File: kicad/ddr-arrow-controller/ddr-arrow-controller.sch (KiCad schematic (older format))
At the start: 50 parts

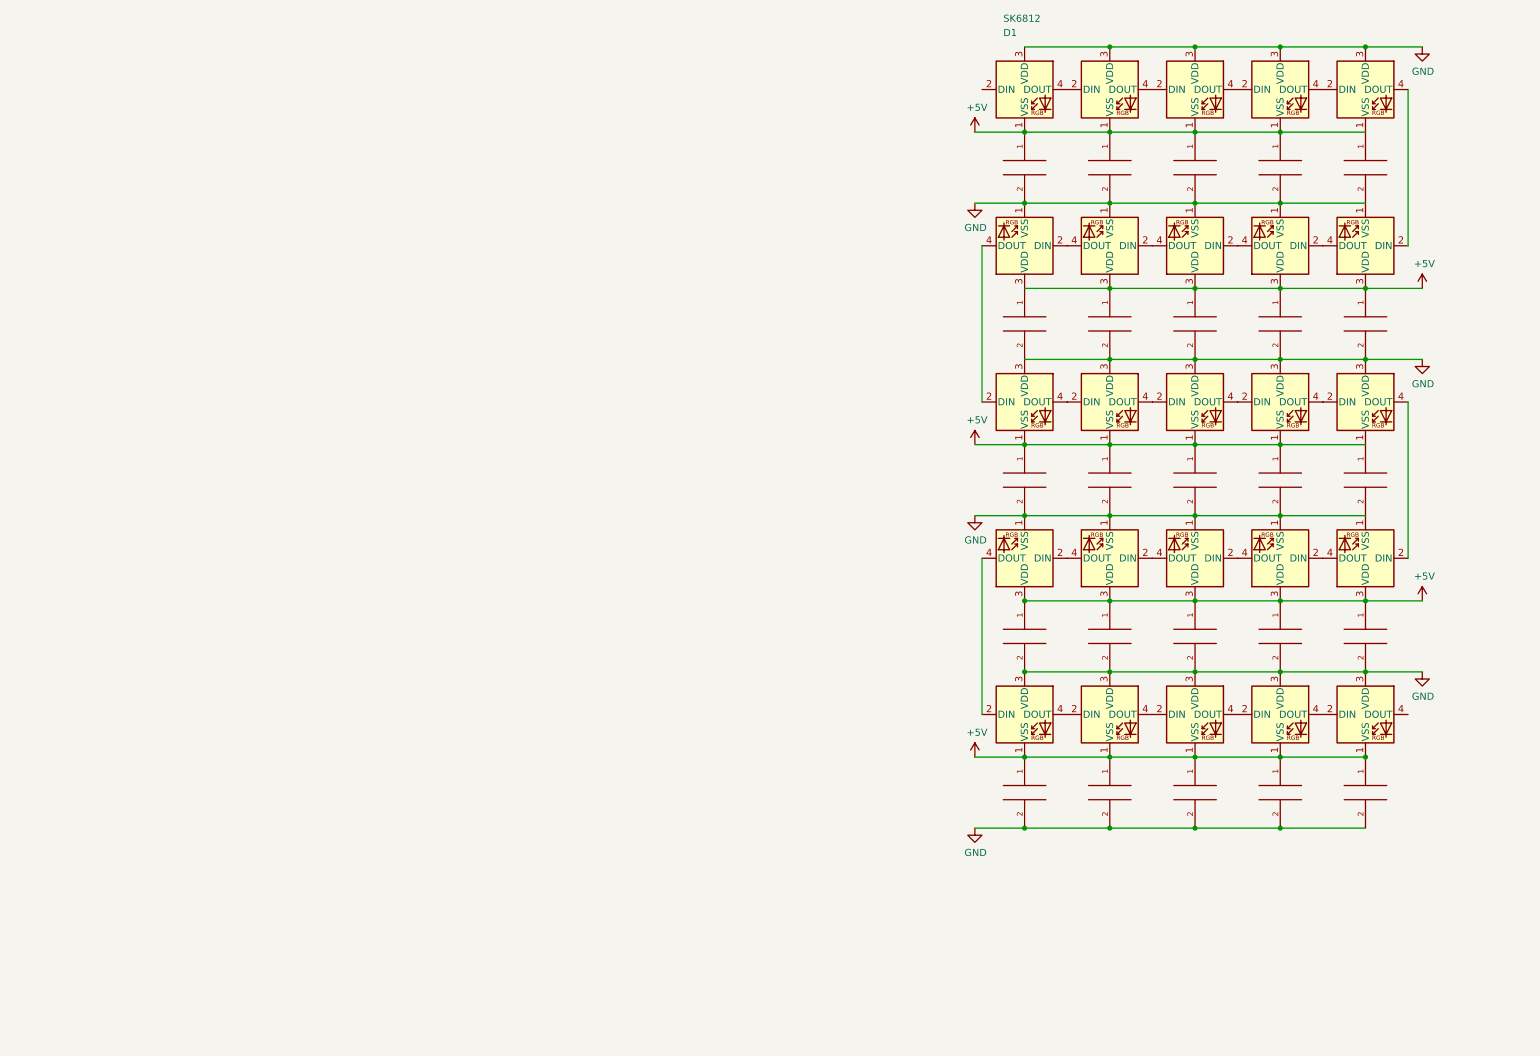
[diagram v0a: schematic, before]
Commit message: Schematic Updates
Placed microcontroller, CANBus chips, power regulator.
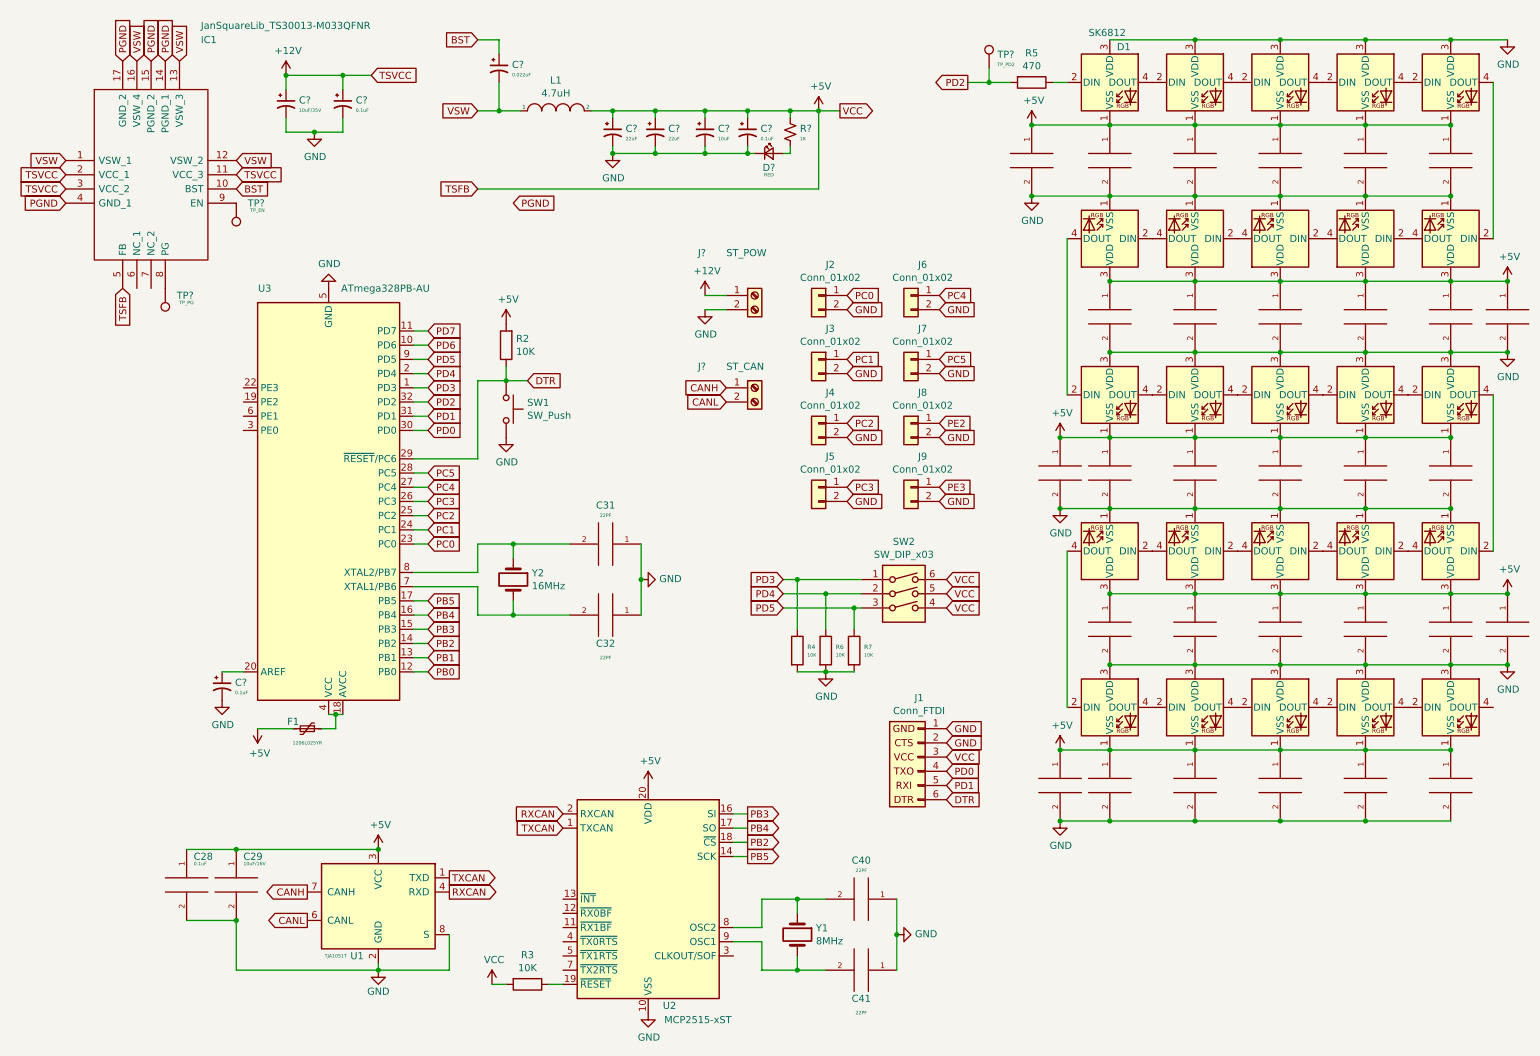
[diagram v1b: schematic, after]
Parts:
- added C28: 0.1uF, symbol pspice:CAP
- added C29: 10uF/16V, symbol pspice:CAP
- added C31, C32, C40, C41: 22PF, symbol pspice:CAP
- added C35, C36, C37, C38, C39: 1000uF, Capacitor_SMD:C_0805_2012Metric_Pad1.15x1.40mm_HandSolder, symbol pspice:CAP
- added C?: 0.022uF, symbol Device:CP1_Small
- added C?: 10uF/35V, symbol Device:CP1_Small
- added C? (x3): 0.1uF, symbol Device:CP1_Small
- added C? (x2): 22uF, symbol Device:CP1_Small
- added C?: 10uF, symbol Device:CP1_Small
- added D?: RED, symbol Device:LED_Small
- added F1: 1206L025YR, Fuse:Fuse_1206_3216Metric, symbol Device:Polyfuse_Small
- added IC1: JanSquareLib_TS30013-M033QFNR, QFN50P300X300X100-17N-D, symbol TS30013:JanSquareLib_TS30013-M033QFNR
- added J1: Conn_FTDI, symbol conn_ftdi:Conn_FTDI
- added J2, J3, J4, J5, J6, J7, J8, J9: Conn_01x02, symbol Connector_Generic:Conn_01x02
- added J?: ST_POW, symbol Connector:Screw_Terminal_01x02
- added J?: ST_CAN, symbol Connector:Screw_Terminal_01x02
- added L1: 4.7uH, symbol pspice:INDUCTOR
- added R2, R3, R4, R6, R7: 10K, symbol Device:R
- added R5: 470, symbol Device:R
- added R?: 1K, symbol Device:R_Small_US
- added SW1: SW_Push, symbol Switch:SW_Push
- added SW2: SW_DIP_x03, symbol Switch:SW_DIP_x03
- added TP?: TP_PG, symbol TS30013:Connector_TestPoint
- added TP?: TP_EN, symbol TS30013:Connector_TestPoint
- added TP?: TP_PD2, symbol TS30013:Connector_TestPoint
- added U1: TJA1051T, Package_SO:SOIC-8_3.9x4.9mm_P1.27mm, symbol Interface_CAN_LIN:TJA1051T
- added U2: MCP2515-xST, Package_SO:TSSOP-20_4.4x6.5mm_P0.65mm, symbol Interface_CAN_LIN:MCP2515-xST
- added U3: ATmega328PB-AU, Package_QFP:TQFP-32_7x7mm_P0.8mm, symbol MCU_Microchip_ATmega:ATmega328PB-AU
- added Y1: 8MHz, Crystal:Crystal_SMD_5032-2Pin_5.0x3.2mm_HandSoldering, symbol Device:Crystal
- added Y2: 16MHz, Crystal:Crystal_SMD_5032-2Pin_5.0x3.2mm_HandSoldering, symbol Device:Crystal
- renumbered C2 to C42, C5 to C43
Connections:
- net +5V: now also C28.1, C29.1, C35.1, C36.1, C37.1, C38.1, C39.1, C?.1, C?.1, C?.1, C?.1, F1.2, IC1.5 (FB), J1.3 (Pin_3), L1.2, R2.2, R3.2, R?.1, SW2.4, SW2.5, SW2.6, U1.3 (VCC), U2.20 (VDD)
- net GND: now also C28.2, C29.2, C31.1, C32.1, C35.2, C36.2, C37.2, C38.2, C39.2, C40.1, C41.1, C?.2, C?.2, C?.2, C?.2, C?.2, C?.2, C?.2, D?.1 (K), J1.1 (Pin_1), J1.2 (Pin_2), J2.2 (Pin_2), J3.2 (Pin_2), J4.2 (Pin_2), J5.2 (Pin_2), J6.2 (Pin_2), J7.2 (Pin_2), J8.2 (Pin_2), J9.2 (Pin_2), J?.2 (Pin_2), R4.2, R6.2, R7.2, SW1.2, U1.2 (GND), U1.8 (S), U2.10 (VSS), U3.21 (GND), U3.5 (GND)
- net at D1.2 (DIN): now also R5.1
- new net: R3.1, U2.19 (~RESET)
- new net: C40.2, U2.8 (OSC2), Y1.1
- new net: C41.2, U2.9 (OSC1), Y1.2
- new net: F1.1, U3.18 (AVCC), U3.4 (VCC)
- new net: C?.1, U3.20 (AREF)
- new net: C32.2, U3.7 (XTAL1/PB6), Y2.2
- new net: C31.2, U3.8 (XTAL2/PB7), Y2.1
- new net: IC1.8 (PG), TP?.1
- new net: IC1.9 (EN), TP?.1
- new net: D?.2 (A), R?.2
- new net +12V: C?.1, C?.1, IC1.11 (VCC_3), IC1.2 (VCC_1), IC1.3 (VCC_2), J?.1 (Pin_1)
- new net BST: C?.1, IC1.10 (BST)
- new net CANH: J?.1 (Pin_1), U1.7 (CANH)
- new net CANL: J?.2 (Pin_2), U1.6 (CANL)
- new net DTR: J1.6 (Pin_6), R2.1, SW1.1, U3.29 (~RESET~/PC6)
- new net PB0: U3.12 (PB0)
- new net PB1: U3.13 (PB1)
- new net PB2: U2.18 (~CS), U3.14 (PB2)
- new net PB3: U2.16 (SI), U3.15 (PB3)
- new net PB4: U2.17 (SO), U3.16 (PB4)
- new net PB5: U2.14 (SCK), U3.17 (PB5)
- new net PC0: J2.1 (Pin_1), U3.23 (PC0)
- new net PC1: J3.1 (Pin_1), U3.24 (PC1)
- new net PC2: J4.1 (Pin_1), U3.25 (PC2)
- new net PC3: J5.1 (Pin_1), U3.26 (PC3)
- new net PC4: J6.1 (Pin_1), U3.27 (PC4)
- new net PC5: J7.1 (Pin_1), U3.28 (PC5)
- new net PD0: J1.4 (Pin_4), U3.30 (PD0)
- new net PD1: J1.5 (Pin_5), U3.31 (PD1)
- new net PD2: R5.2, TP?.1, U3.32 (PD2)
- new net PD3: R4.1, SW2.1, U3.1 (PD3)
- new net PD4: R6.1, SW2.2, U3.2 (PD4)
- new net PD5: R7.1, SW2.3, U3.9 (PD5)
- new net PD6: U3.10 (PD6)
- new net PD7: U3.11 (PD7)
- new net PE2: J8.1 (Pin_1)
- new net PE3: J9.1 (Pin_1)
- new net PGND: IC1.14 (PGND_1), IC1.15 (PGND_2), IC1.17 (GND_2), IC1.4 (GND_1)
- new net RXCAN: U1.4 (RXD), U2.2 (RXCAN)
- new net TXCAN: U1.1 (TXD), U2.1 (TXCAN)
- new net VSW: C?.2, IC1.1 (VSW_1), IC1.12 (VSW_2), IC1.13 (VSW_3), IC1.16 (VSW_4), L1.1
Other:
- moved on the sheet: D1

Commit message: Board layout v1 complete
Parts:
- removed C32, C40, C41: 22PF, symbol pspice:CAP
- removed C36, C37, C38, C39: 1000uF, Capacitor_SMD:C_0805_2012Metric_Pad1.15x1.40mm_HandSolder, symbol pspice:CAP
- removed J1: Conn_FTDI, symbol conn_ftdi:Conn_FTDI
- removed J6, J7, J8, J9: Conn_01x02, symbol Connector_Generic:Conn_01x02
- removed R2, R3, R4, R6, R7: 10K, symbol Device:R
- removed R5: 470, symbol Device:R
- removed SW2: SW_DIP_x03, symbol Switch:SW_DIP_x03
- removed TP?: TP_PD2, symbol TS30013:Connector_TestPoint
- removed U2: MCP2515-xST, Package_SO:TSSOP-20_4.4x6.5mm_P0.65mm, symbol Interface_CAN_LIN:MCP2515-xST
- removed Y1: 8MHz, Crystal:Crystal_SMD_5032-2Pin_5.0x3.2mm_HandSoldering, symbol Device:Crystal
- removed Y2: 16MHz, Crystal:Crystal_SMD_5032-2Pin_5.0x3.2mm_HandSoldering, symbol Device:Crystal
- added J10: OPTO, Connector_JST:JST_PH_B2B-PH-K_1x02_P2.00mm_Vertical, symbol Connector_Generic:Conn_01x02
- added J13: Step Sensor, Connector_JST:JST_PH_B2B-PH-K_1x02_P2.00mm_Vertical, symbol Connector_Generic:Conn_01x02
- added J6: AVR-ISP-6, Connector_PinHeader_2.54mm:PinHeader_2x03_P2.54mm_Vertical, symbol Connector:AVR-ISP-6
- added JP1: LED_EN, Jumper:SolderJumper-2_P1.3mm_Bridged_Pad1.0x1.5mm, symbol Jumper:SolderJumper_2_Bridged
- added JP2: Jumper_NO_Small, Connector_PinSocket_2.54mm:PinSocket_1x02_P2.54mm_Vertical, symbol Device:Jumper_NO_Small
- added R1, R10, R2, R6, R7, R8: 10K, Resistor_SMD:R_0805_2012Metric_Pad1.15x1.40mm_HandSolder, symbol Device:R_Small_US
- added R11, R12, R3: 560, Resistor_SMD:R_0805_2012Metric_Pad1.15x1.40mm_HandSolder, symbol Device:R_Small_US
- added R13: 120, Resistor_SMD:R_0805_2012Metric_Pad1.15x1.40mm_HandSolder, symbol Device:R_Small_US
- added R4: 1K, Resistor_SMD:R_0805_2012Metric_Pad1.15x1.40mm_HandSolder, symbol Device:R_Small_US
- added R9: 470, Resistor_SMD:R_0805_2012Metric_Pad1.15x1.40mm_HandSolder, symbol Device:R_Small_US
- added SW2: SW_DIP_x04, Button_Switch_SMD:SW_DIP_SPSTx04_Slide_9.78x12.34mm_W8.61mm_P2.54mm, symbol Switch:SW_DIP_x04
- added TP10: PC5, TestPoint:TestPoint_Pad_1.0x1.0mm, symbol ddr-arrow-controller-rescue:Connector_TestPoint-TS30013
- added TP11: 5V, TestPoint:TestPoint_Pad_D2.0mm, symbol ddr-arrow-controller-rescue:Connector_TestPoint-TS30013
- added TP12: GND, TestPoint:TestPoint_Pad_D2.0mm, symbol ddr-arrow-controller-rescue:Connector_TestPoint-TS30013
- added TP13: PD0, TestPoint:TestPoint_Pad_D2.0mm, symbol ddr-arrow-controller-rescue:Connector_TestPoint-TS30013
- added TP14: PD1, TestPoint:TestPoint_Pad_D2.0mm, symbol ddr-arrow-controller-rescue:Connector_TestPoint-TS30013
- added TP3: PE2, TestPoint:TestPoint_Pad_1.0x1.0mm, symbol ddr-arrow-controller-rescue:Connector_TestPoint-TS30013
- added TP4: PE3, TestPoint:TestPoint_Pad_1.0x1.0mm, symbol ddr-arrow-controller-rescue:Connector_TestPoint-TS30013
- added TP5: PB1, TestPoint:TestPoint_Pad_D2.0mm, symbol ddr-arrow-controller-rescue:Connector_TestPoint-TS30013
- added TP6: PB0, TestPoint:TestPoint_Pad_D2.0mm, symbol ddr-arrow-controller-rescue:Connector_TestPoint-TS30013
- added TP7: PE1, TestPoint:TestPoint_Pad_1.0x1.0mm, symbol ddr-arrow-controller-rescue:Connector_TestPoint-TS30013
- added TP8: PC4, TestPoint:TestPoint_Pad_1.0x1.0mm, symbol ddr-arrow-controller-rescue:Connector_TestPoint-TS30013
- added U2: MCP2515-xSO, Package_SO:SOIC-18W_7.5x11.6mm_P1.27mm, symbol Interface_CAN_LIN:MCP2515-xSO
- added U4, U5: TLP290, Package_SO:SOP-4_4.4x2.6mm_P1.27mm, symbol Isolator:TLP290
- added Y1: 16MHz, Crystal:Resonator_SMD_muRata_CSTxExxV-3Pin_3.0x1.1mm_HandSoldering, symbol Device:Resonator_Small
- added Y2: 8MHz, Crystal:Resonator_SMD_muRata_CSTxExxV-3Pin_3.0x1.1mm_HandSoldering, symbol Device:Resonator_Small
- C2, C26, C27, C30, C33, C44: renamed from C?; footprint (none) -> Capacitor_SMD:C_0805_2012Metric_Pad1.15x1.40mm_HandSolder
- C28: footprint (none) -> Capacitor_SMD:C_0805_2012Metric_Pad1.15x1.40mm_HandSolder
- C29: footprint (none) -> Capacitor_SMD:C_1206_3216Metric_Pad1.42x1.75mm_HandSolder
- C31: value 22PF -> 22uF; footprint (none) -> Capacitor_SMD:C_0805_2012Metric_Pad1.15x1.40mm_HandSolder
- C34, C5: renamed from C?; footprint (none) -> Capacitor_SMD:C_1206_3216Metric_Pad1.42x1.75mm_HandSolder
- C35: footprint Capacitor_SMD:C_0805_2012Metric_Pad1.15x1.40mm_HandSolder -> Capacitor_SMD:C_Elec_10x10.2
- D26: renamed from D?; footprint (none) -> LED_SMD:LED_0805_2012Metric
- IC1: footprint QFN50P300X300X100-17N-D -> TS30013:QFN50P300X300X100-17N; symbol TS30013:JanSquareLib_TS30013-M033QFNR -> ddr-arrow-controller-rescue:JanSquareLib_TS30013-M033QFNR-TS30013
- J11: renamed from J?; footprint (none) -> Connector_Molex:Molex_Mini-Fit_Jr_5569-02A2_2x01_P4.20mm_Horizontal
- J12: renamed from J?; footprint (none) -> TerminalBlock_Phoenix:TerminalBlock_Phoenix_MKDS-1,5-2_1x02_P5.00mm_Horizontal
- J2: value Conn_01x02 -> A0; footprint (none) -> Connector_JST:JST_PH_B2B-PH-K_1x02_P2.00mm_Vertical
- J3: value Conn_01x02 -> A1; footprint (none) -> Connector_JST:JST_PH_B2B-PH-K_1x02_P2.00mm_Vertical
- J4: value Conn_01x02 -> A2; footprint (none) -> Connector_JST:JST_PH_B2B-PH-K_1x02_P2.00mm_Vertical
- J5: value Conn_01x02 -> A3; footprint (none) -> Connector_JST:JST_PH_B2B-PH-K_1x02_P2.00mm_Vertical
- L1: footprint (none) -> Inductor_SMD:L_Taiyo-Yuden_NR-80xx_HandSoldering
- R5: renamed from R?; footprint (none) -> Resistor_SMD:R_0805_2012Metric_Pad1.15x1.40mm_HandSolder
- SW1: footprint (none) -> Button_Switch_SMD:SW_SPST_CK_RS282G05A3
- TP1, TP2: renamed from TP?; footprint (none) -> TestPoint:TestPoint_Pad_1.0x1.0mm; symbol TS30013:Connector_TestPoint -> ddr-arrow-controller-rescue:Connector_TestPoint-TS30013
- renumbered D2 to D10, D3 to D11, D8 to D12, D18 to D14, D23 to D15, D24 to D16, D19 to D17, D14 to D18, D9 to D19, D6 to D2, D4 to D20, D5 to D21, D10 to D22, D15 to D23, D20 to D24, D11 to D3, D16 to D4, D21 to D5, D22 to D6, D17 to D7, D12 to D8, D7 to D9
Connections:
- net PGND is gone; now on net GND: IC1.14 (PGND_1), IC1.15 (PGND_2), IC1.17 (GND_2), IC1.4 (GND_1)
- net +12V: now also J11.2 (Pin_2); no longer J11.1 (Pin_1)
- net +5V: now also C31.1, F1.1, U3.18 (AVCC), U3.4 (VCC), J6.2 (VCC), JP1.1 (A), R1.1, R2.2, R4.1, SW2.5, SW2.6, SW2.7, SW2.8, TP11.1, U2.18 (VDD); no longer R5.1
- net CANH: now also J12.2 (Pin_2), JP2.1; no longer J12.1 (Pin_1)
- net CANL: now also J12.1 (Pin_1), R13.2; no longer J12.2 (Pin_2)
- net DTR: now also J6.5 (~RST), R1.2
- net GND: now also C31.2, J11.1 (Pin_1), J6.6 (GND), R10.2, R6.2, R7.2, R8.2, TP12.1, U2.9 (VSS), U4.3, U5.2, Y1.2, Y2.2; no longer C31.1, J11.2 (Pin_2)
- net PB0: now also TP6.1
- net PB1: now also TP5.1
- net PB2: now also U2.16 (~CS)
- net PB3: now also J6.4 (MOSI), U2.14 (SI)
- net PB4: now also J6.1 (MISO), U2.15 (SO)
- net PB5: now also J6.3 (SCK), U2.13 (SCK)
- net PC4: now also TP8.1
- net PC5: now also TP10.1
- net PD0: now also TP13.1
- net PD1: now also TP14.1
- net PD2: now also R9.2
- net PD3: now also R8.1, SW2.4
- net PD4: now also R7.1, SW2.3
- net PD5: now also R6.1, SW2.2
- net PD6: now also R10.1, SW2.1
- net PD7: now also R4.2, U4.4
- net PE2: now also U3.19 (PE2), TP3.1
- net PE3: now also U3.22 (PE3), TP4.1
- net RXCAN: now also U2.2 (RXCAN)
- net TXCAN: now also U2.1 (TXCAN)
- net at D1.2 (DIN): now also R9.1
- net PE0: now reaches U3.3 (PE0)
- net PE0: now also R11.2
- net PE1: now reaches U3.6 (PE1)
- net PE1: now also TP7.1
- net at U3.7 (XTAL1/PB6): now also Y1.1
- net at U3.8 (XTAL2/PB7): now also Y1.3; no longer C31.2
- new net: U2.8 (OSC1), Y2.1
- new net: U2.7 (OSC2), Y2.3
- new net: R2.1, U2.17 (~RESET)
- new net: JP1.2 (B), R5.1
- new net: J13.1 (Pin_1), R12.1
- new net: J13.2 (Pin_2), U5.3
- new net: R11.1, U5.1
- new net: R12.2, U5.4
- new net: JP2.2, R13.1
- new net: J10.1 (Pin_1), R3.2
- new net: J10.2 (Pin_2), U4.2
- new net: R3.1, U4.1
- no-connect marks 0 -> 8
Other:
- moved on the sheet: C2, C26, C28, C29, C5, D26, F1, R5, SW1, TP1, TP2, U1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

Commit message: Rerouted PCB
Fixed pcb plains. Fixed grounds. Fixed rounded pads. Exported Gerber files.
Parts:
- removed C1, C10, C11, C12, C13, C14, C15, C16, C17, C18, C19, C20, C21, C22, C23, C24, C25, C3, C4, C42, C43, C6, C7, C8, C9: 0.1uF, Capacitor_SMD:C_0805_2012Metric_Pad1.15x1.40mm_HandSolder, symbol pspice:CAP
- removed C26: 0.1uF, Capacitor_SMD:C_0805_2012Metric_Pad1.15x1.40mm_HandSolder, symbol Device:CP1_Small
- removed C31: 22uF, Capacitor_SMD:C_0805_2012Metric_Pad1.15x1.40mm_HandSolder, symbol pspice:CAP
- removed F1: 1206L025YR, Fuse:Fuse_1206_3216Metric, symbol Device:Polyfuse_Small
- removed TP10: PC5, TestPoint:TestPoint_Pad_1.0x1.0mm, symbol ddr-arrow-controller-rescue:Connector_TestPoint-TS30013
- removed TP11: 5V, TestPoint:TestPoint_Pad_D2.0mm, symbol ddr-arrow-controller-rescue:Connector_TestPoint-TS30013
- removed TP12: GND, TestPoint:TestPoint_Pad_D2.0mm, symbol ddr-arrow-controller-rescue:Connector_TestPoint-TS30013
- added C1, C10, C11, C12, C13, C14, C15, C16, C17, C18, C19, C20, C21, C22, C23, C24, C25, C3, C31, C32, C4, C6, C7, C8, C9: 0.1uF, Capacitor_SMD:C_0805_2012Metric_Pad1.15x1.40mm_HandSolder, symbol Device:C_Small
- added TP9: PD2, TestPoint:TestPoint_Pad_D1.0mm, symbol ddr-arrow-controller-rescue:Connector_TestPoint-TS30013
- C35: symbol pspice:CAP -> Device:CP1_Small
- TP13, TP14: footprint TestPoint:TestPoint_Pad_D2.0mm -> TestPoint:TestPoint_Pad_D1.0mm
- TP4: value PE3 -> PC4
- TP8: value PC4 -> PC5
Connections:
- net +5V: now also D1.3 (VDD), D11.3 (VDD), D12.3 (VDD), D13.3 (VDD), D14.3 (VDD), D15.3 (VDD), D2.3 (VDD), D21.3 (VDD), D22.3 (VDD), D23.3 (VDD), D24.3 (VDD), D25.3 (VDD), D3.3 (VDD), D4.3 (VDD), D5.3 (VDD), C1.1, C10.1, C11.1, C12.1, C13.1, C14.1, C15.1, C16.1, C17.1, C18.1, C19.1, C20.1, C21.1, C22.1, C23.1, C24.1, C25.1, C3.1, C31.1, C32.1, C4.1, C6.1, C7.1, C8.1, C9.1; no longer D1.1 (VSS), D11.1 (VSS), D12.1 (VSS), D13.1 (VSS), D14.1 (VSS), D15.1 (VSS), D2.1 (VSS), D21.1 (VSS), D22.1 (VSS), D23.1 (VSS), D24.1 (VSS), D25.1 (VSS), D3.1 (VSS), D4.1 (VSS), D5.1 (VSS)
- net GND: now also D1.1 (VSS), D11.1 (VSS), D12.1 (VSS), D13.1 (VSS), D14.1 (VSS), D15.1 (VSS), D2.1 (VSS), D21.1 (VSS), D22.1 (VSS), D23.1 (VSS), D24.1 (VSS), D25.1 (VSS), D3.1 (VSS), D4.1 (VSS), D5.1 (VSS), C1.2, C10.2, C11.2, C12.2, C13.2, C14.2, C15.2, C16.2, C17.2, C18.2, C19.2, C20.2, C21.2, C22.2, C23.2, C24.2, C25.2, C3.2, C31.2, C32.2, C4.2, C6.2, C7.2, C8.2, C9.2; no longer D1.3 (VDD), D11.3 (VDD), D12.3 (VDD), D13.3 (VDD), D14.3 (VDD), D15.3 (VDD), D2.3 (VDD), D21.3 (VDD), D22.3 (VDD), D23.3 (VDD), D24.3 (VDD), D25.3 (VDD), D3.3 (VDD), D4.3 (VDD), D5.3 (VDD)
- net PC4: now also TP4.1; no longer TP8.1
- net PC5: now also TP8.1
- net PD2: now also TP9.1; no longer R9.2
- net PD5: now also R9.2; no longer R6.1, SW2.2
- net PE3: now also R6.1, SW2.2; no longer TP4.1
- no-connect marks 8 -> 7
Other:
- moved on the sheet: C27, C30, C33, C34, C44, C5, D1, D26, J10, J13, J6, JP1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
